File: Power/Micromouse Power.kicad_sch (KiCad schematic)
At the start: 35 parts, among them J1 Battery, J2 Conn_02x08_Odd_Even, SW1 SW_SPST, U1 AMS1117-3.3, U2 TP4056, U3 DRV8837, U4 DRV8837

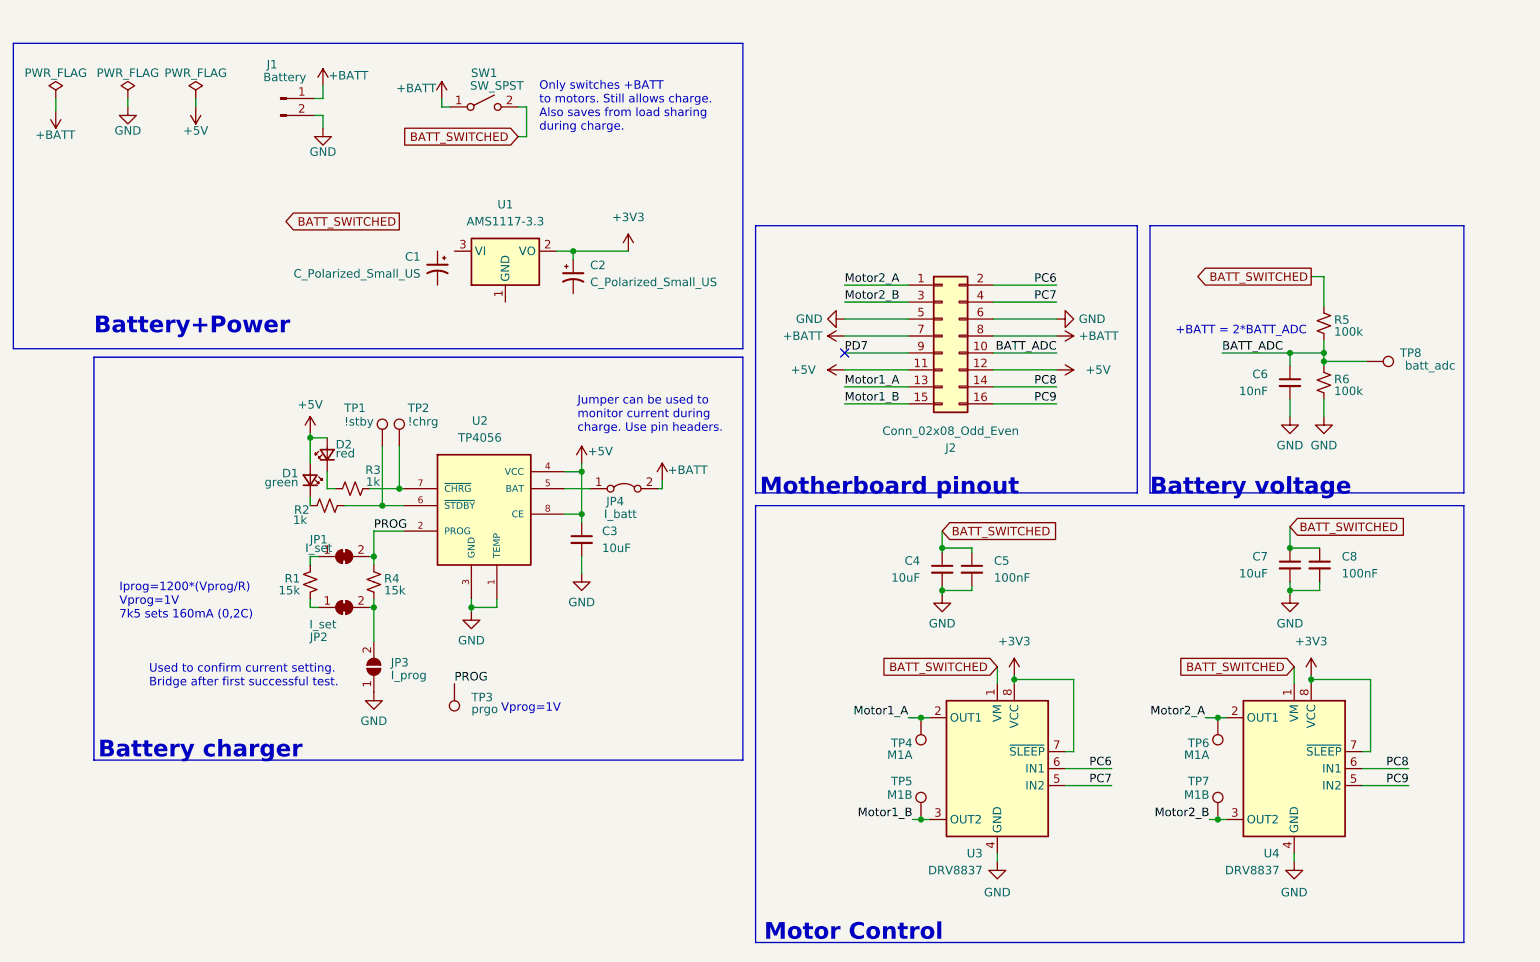
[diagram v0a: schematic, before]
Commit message: Added 3v3 LDO
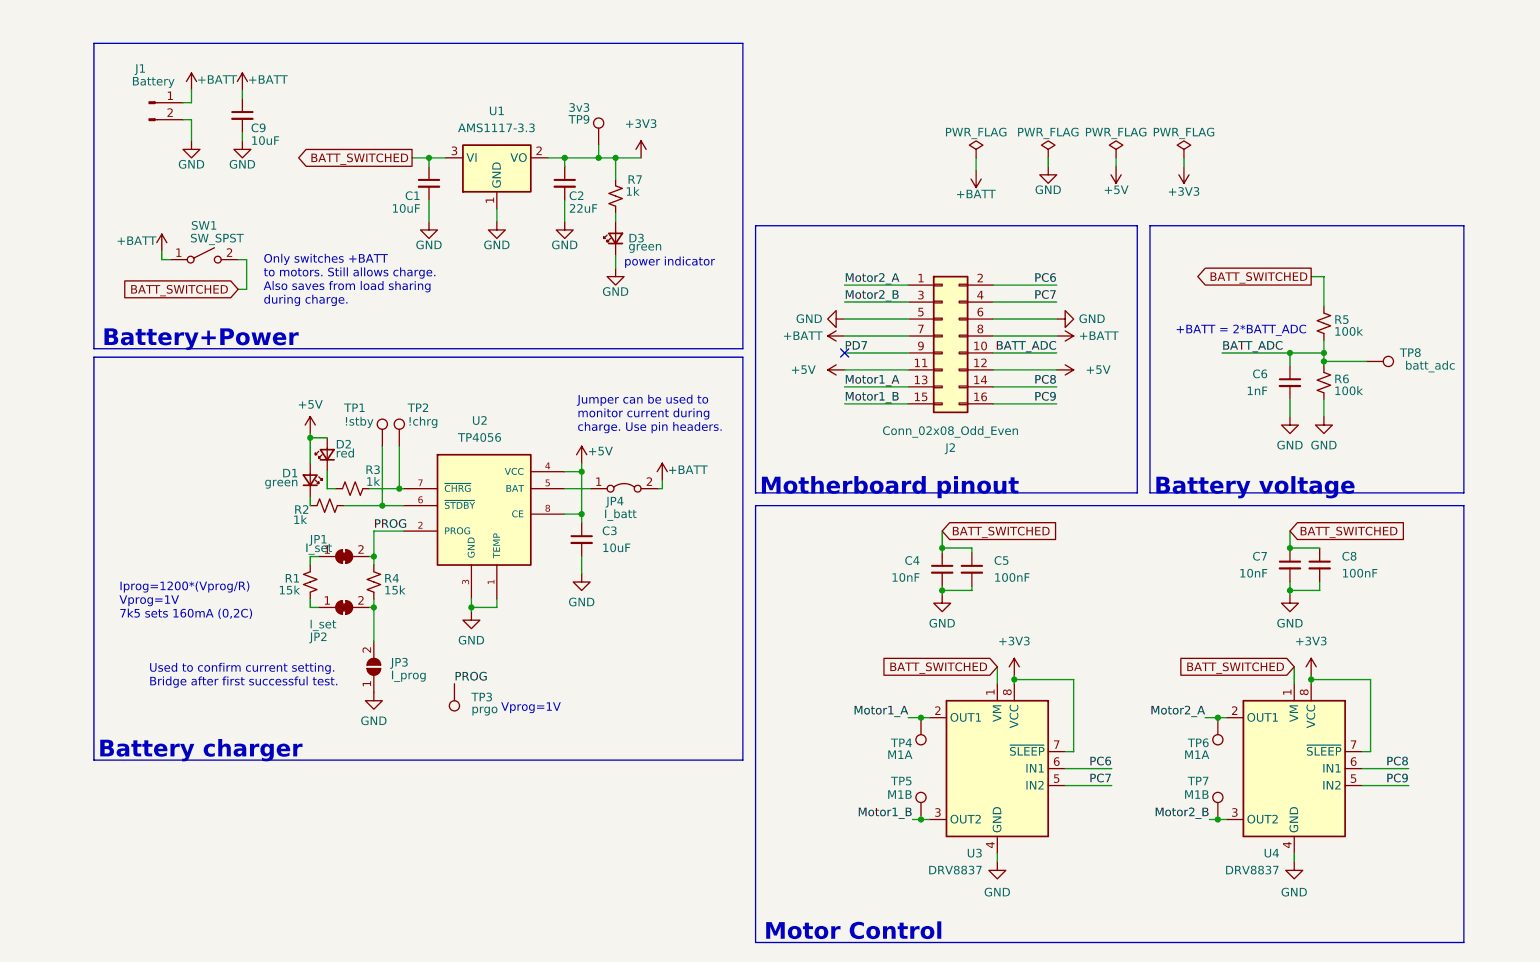
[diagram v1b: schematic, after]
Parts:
- removed C1, C2: C_Polarized_Small_US, symbol Device:C_Polarized_Small_US
- added C1, C9: 10uF, symbol Device:C_Small
- added C2: 22uF, symbol Device:C_Small
- added D3: green, symbol Device:LED_Small
- added R7: 1k, symbol Device:R_Small_US
- added TP9: 3v3, TestPoint:TestPoint_Pad_D1.0mm, symbol Connector:TestPoint
- C4, C7: value 10uF -> 10nF
- C6: value 10nF -> 1nF
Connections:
- net +3V3: now also C2.1, R7.2, TP9.1
- net +BATT: now also C9.1
- net BATT_SWITCHED: now also U1.3 (VI), C1.1
- net GND: now also U1.1 (GND), C1.2, C2.2, C9.2, D3.1 (K)
- new net: D3.2 (A), R7.1
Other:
- note added: "power indicator"
- moved on the sheet: J1, SW1, U1

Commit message: Assigned footprints. Except switch
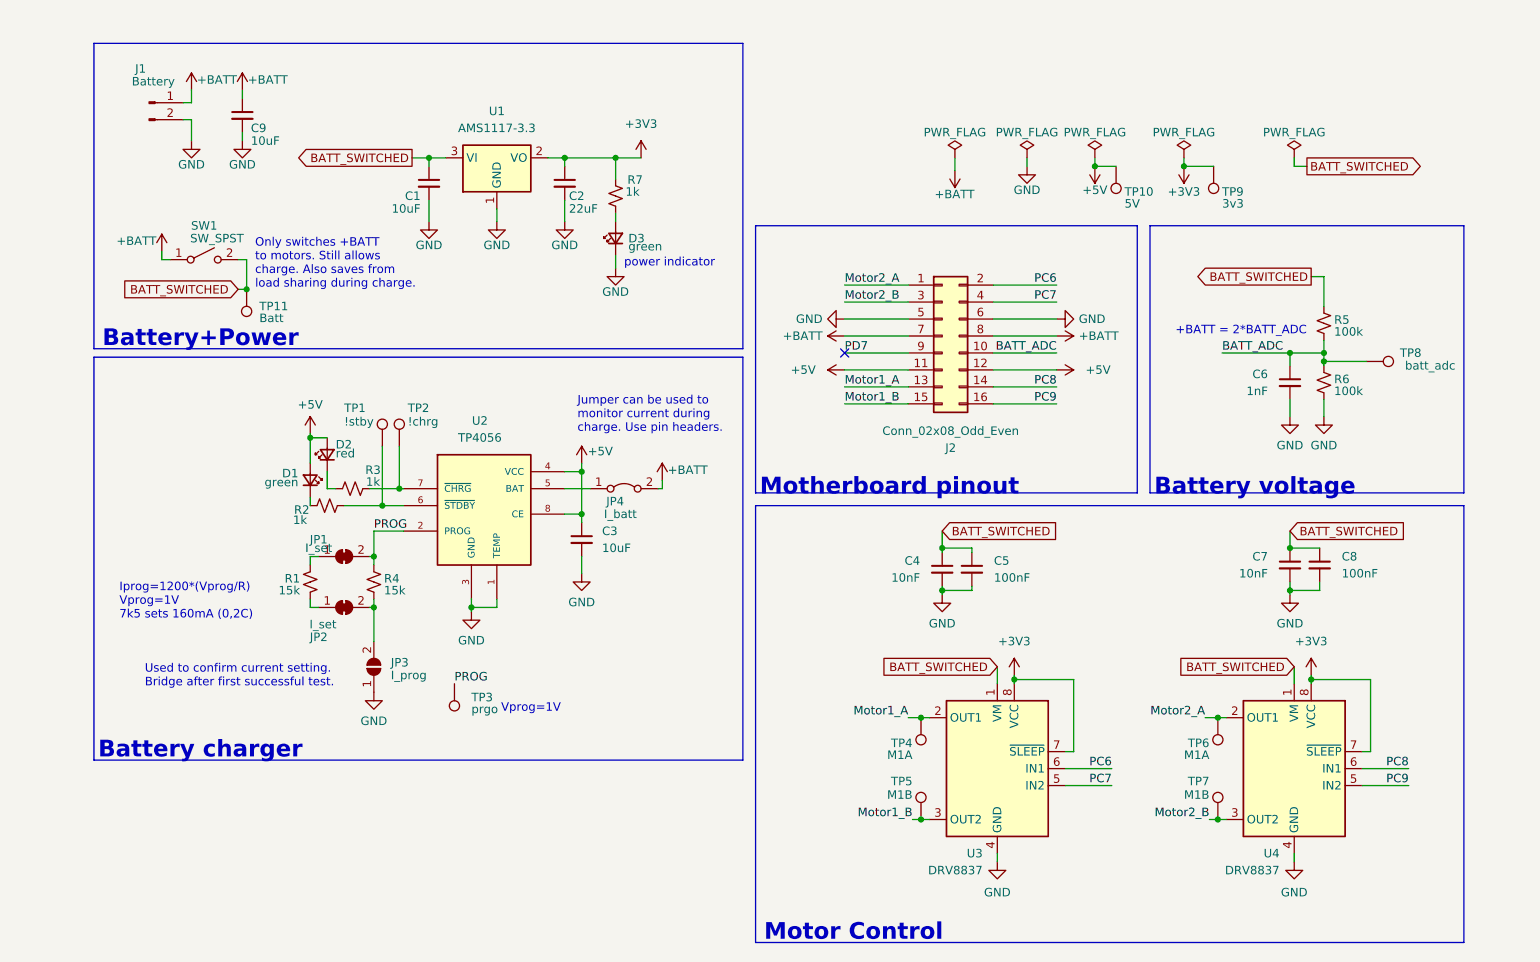
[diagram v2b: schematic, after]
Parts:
- added TP10: 5V, TestPoint:TestPoint_Pad_D1.0mm, symbol Connector:TestPoint
- added TP11: Batt, TestPoint:TestPoint_Pad_D1.0mm, symbol Connector:TestPoint
- C1, C2, C3, C4, C5, C6, C7, C8, C9: footprint (none) -> Capacitor_SMD:C_0603_1608Metric
- D1, D2, D3: footprint (none) -> LED_SMD:LED_0603_1608Metric
- J2, JP4: Populate (none) -> 0
- R1, R4: footprint (none) -> Resistor_SMD:R_0805_2012Metric_Pad1.20x1.40mm_HandSolder
- R2, R3, R5, R6, R7: footprint (none) -> Resistor_SMD:R_0603_1608Metric_Pad0.98x0.95mm_HandSolder
- U1: LCSC (none) -> C6186; Populate (none) -> 1
- U3, U4: LCSC (none) -> C191000; Populate (none) -> 1
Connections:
- net +5V: now also TP10.1
- net BATT_SWITCHED: now also TP11.1
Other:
- moved on the sheet: TP9

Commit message: Updated document details
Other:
- company: (none) -> Group 55
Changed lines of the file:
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@@
     (date "2024-03-18")
     (rev "v0.0.0")
-    (comment 1 "@author Montso Mokake")
-    (comment 2 "@partner Bokang Lepolesa")
+    (company "Group 55")
+    (comment 1 "@author Montso Mokake, MKKMON002")
+    (comment 2 "@partner Bokang Lepolesa, LPLBOK002")
     (comment 3 "@presented_for EEE3088F Project")
   )

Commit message: Added Hor. battery connector. Temp switch ft.
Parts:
- SW1: footprint (none) -> Button_Switch_SMD:Nidec_Copal_CAS-120A
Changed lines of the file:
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@@
       (effects (font (size 1.27 1.27)))
     )
-    (property "Footprint" "" (at 74.93 53.34 0)
+    (property "Footprint" "Button_Switch_SMD:Nidec_Copal_CAS-120A" (at 74.93 53.34 0)
       (effects (font (size 1.27 1.27)) hide)
     )

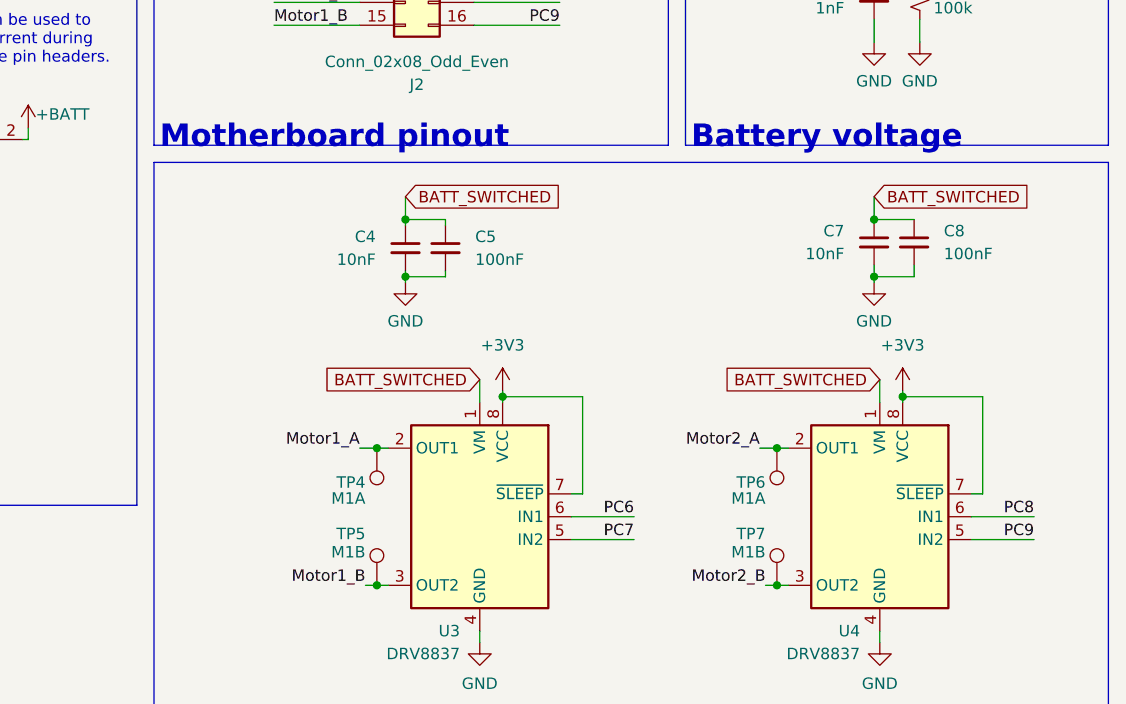
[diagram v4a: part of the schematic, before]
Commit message: Added 3v3 decoup for drv8837
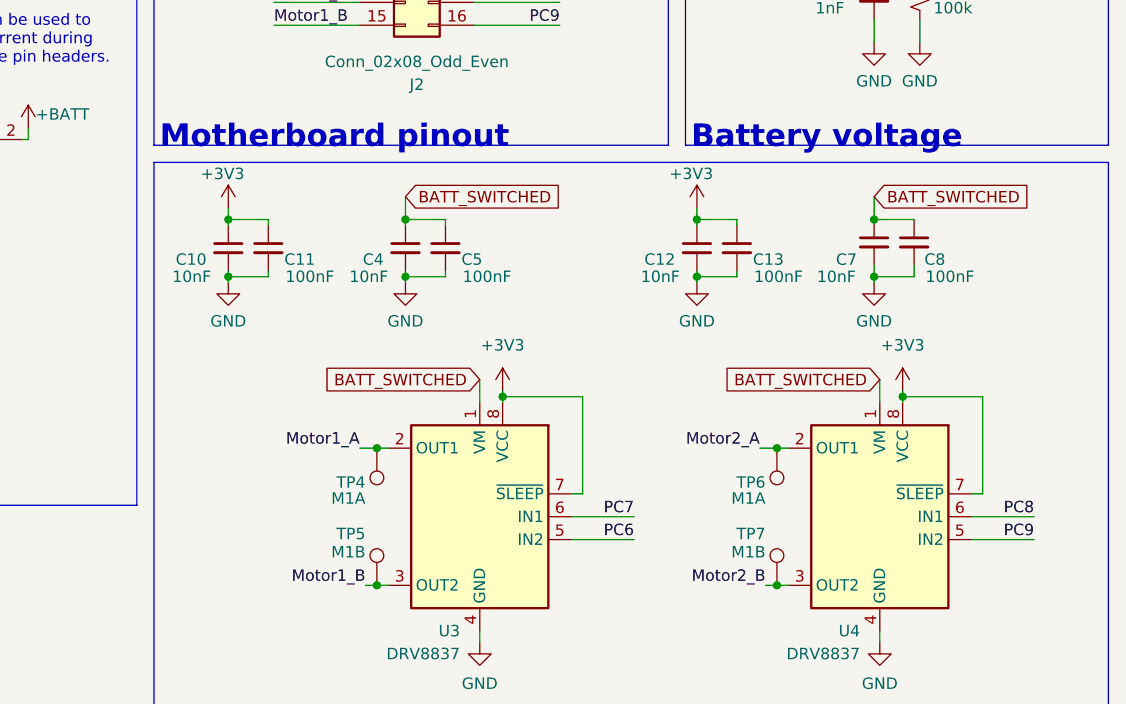
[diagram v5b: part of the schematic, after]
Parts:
- added C10, C12: 10nF, Capacitor_SMD:C_0603_1608Metric, symbol Device:C_Small
- added C11, C13: 100nF, Capacitor_SMD:C_0603_1608Metric, symbol Device:C_Small
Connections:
- net +3V3: now also C10.1, C11.1, C12.1, C13.1
- net GND: now also C10.2, C11.2, C12.2, C13.2
- net PC6: now also U3.5 (IN2); no longer U3.6 (IN1)
- net PC7: now also U3.6 (IN1); no longer U3.5 (IN2)

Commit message: PCB routing optimisation
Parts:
- J2, JP4: Populate 0 -> (none)
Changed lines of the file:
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@@
       (effects (font (size 1.27 1.27)) hide)
     )
-    (property "Populate" "0" (at 185.42 64.77 0)
+    (property "Populate" "" (at 185.42 64.77 0)
       (effects (font (size 1.27 1.27)) hide)
     )
@@
       (effects (font (size 1.27 1.27)) hide)
     )
-    (property "Populate" "0" (at 137.795 87.63 0)
-      (effects (font (size 1.27 1.27)) hide)
-    )
+    (property "Populate" "" (at 137.795 87.63 0)
+      (effects (font (size 1.27 1.27)) hide)
+    )
